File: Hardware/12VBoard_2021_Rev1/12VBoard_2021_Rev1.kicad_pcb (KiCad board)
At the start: 2 copper layers, 178 parts, among them Q1 2N7000, Q2 2N7000, Q3 NTR2101P, Q4 2N7000, Q5 2N7000, Q6 2N7000, Q7 2N7000, SW1 SW_SPDT, U1 LM2576SX-5.0/NOPB, U10 LM5116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

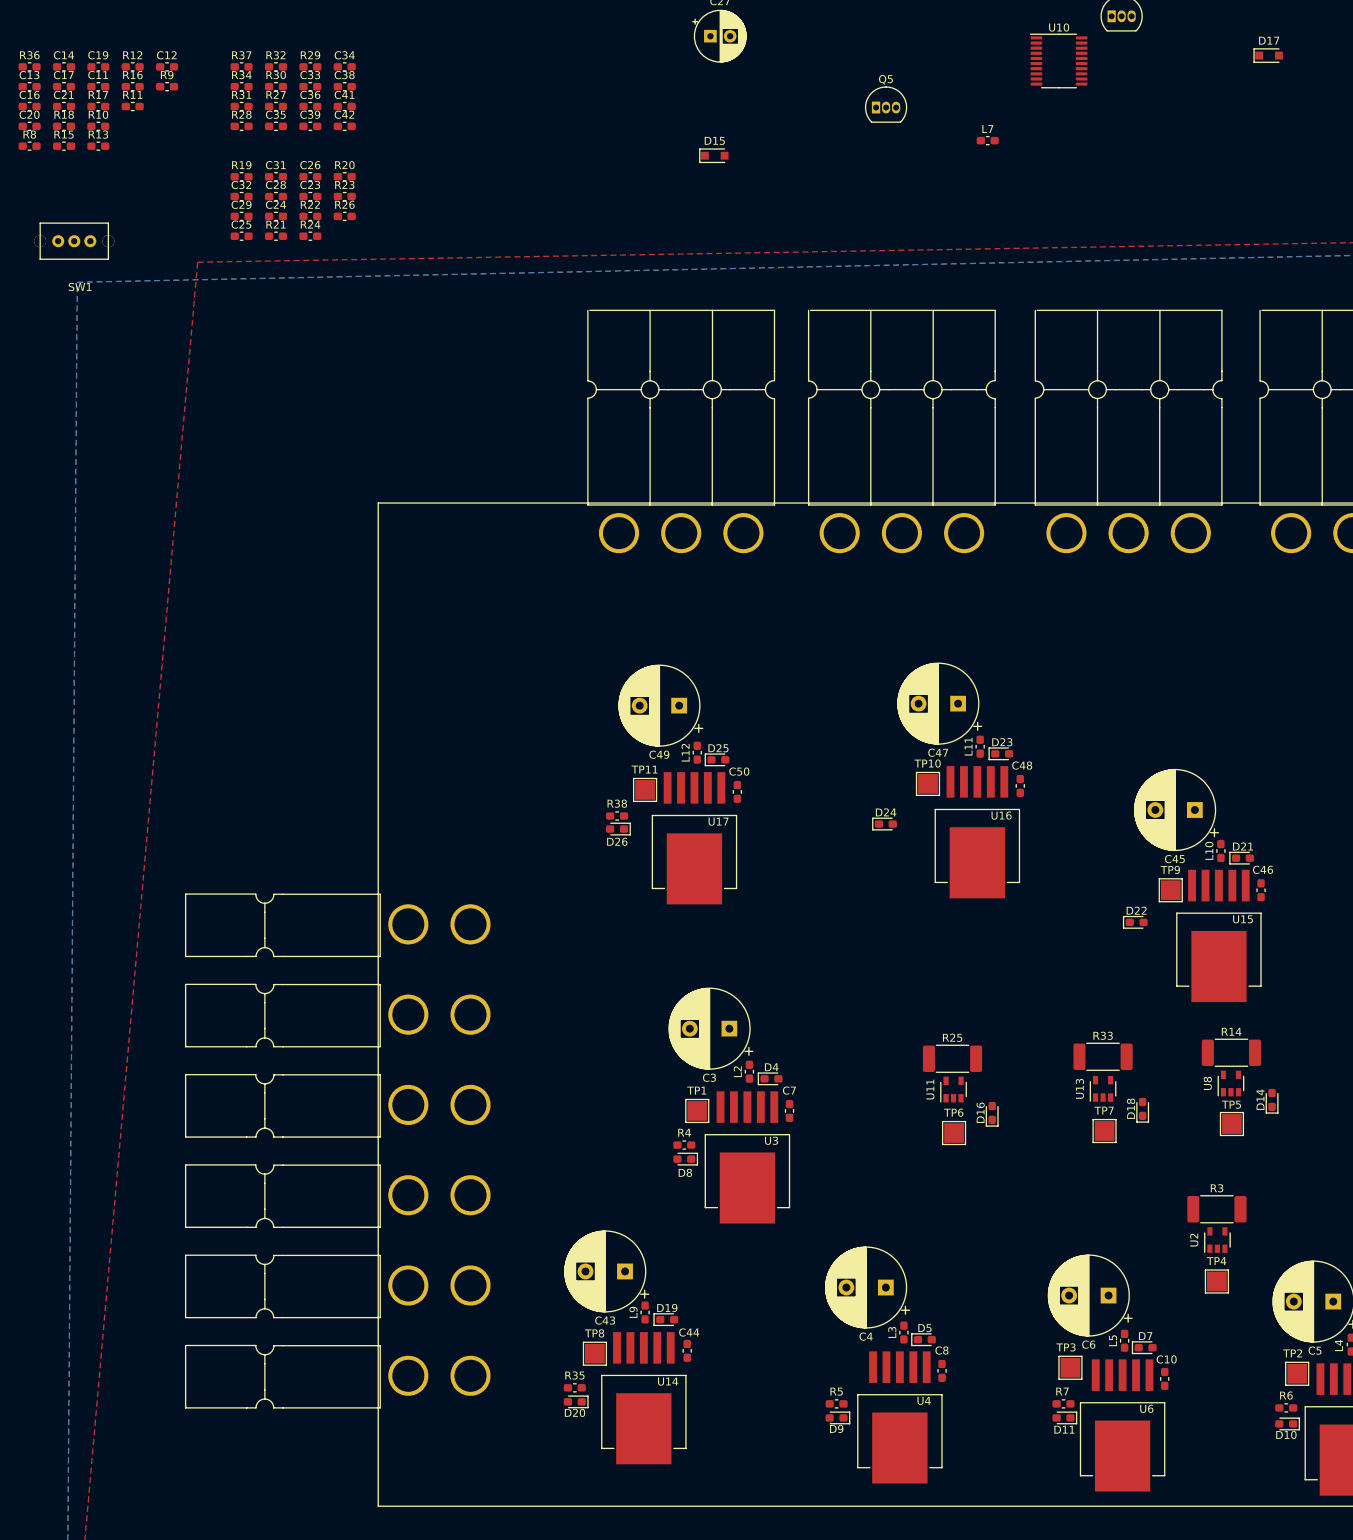
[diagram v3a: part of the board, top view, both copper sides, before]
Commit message: Fixed Nets for andersons
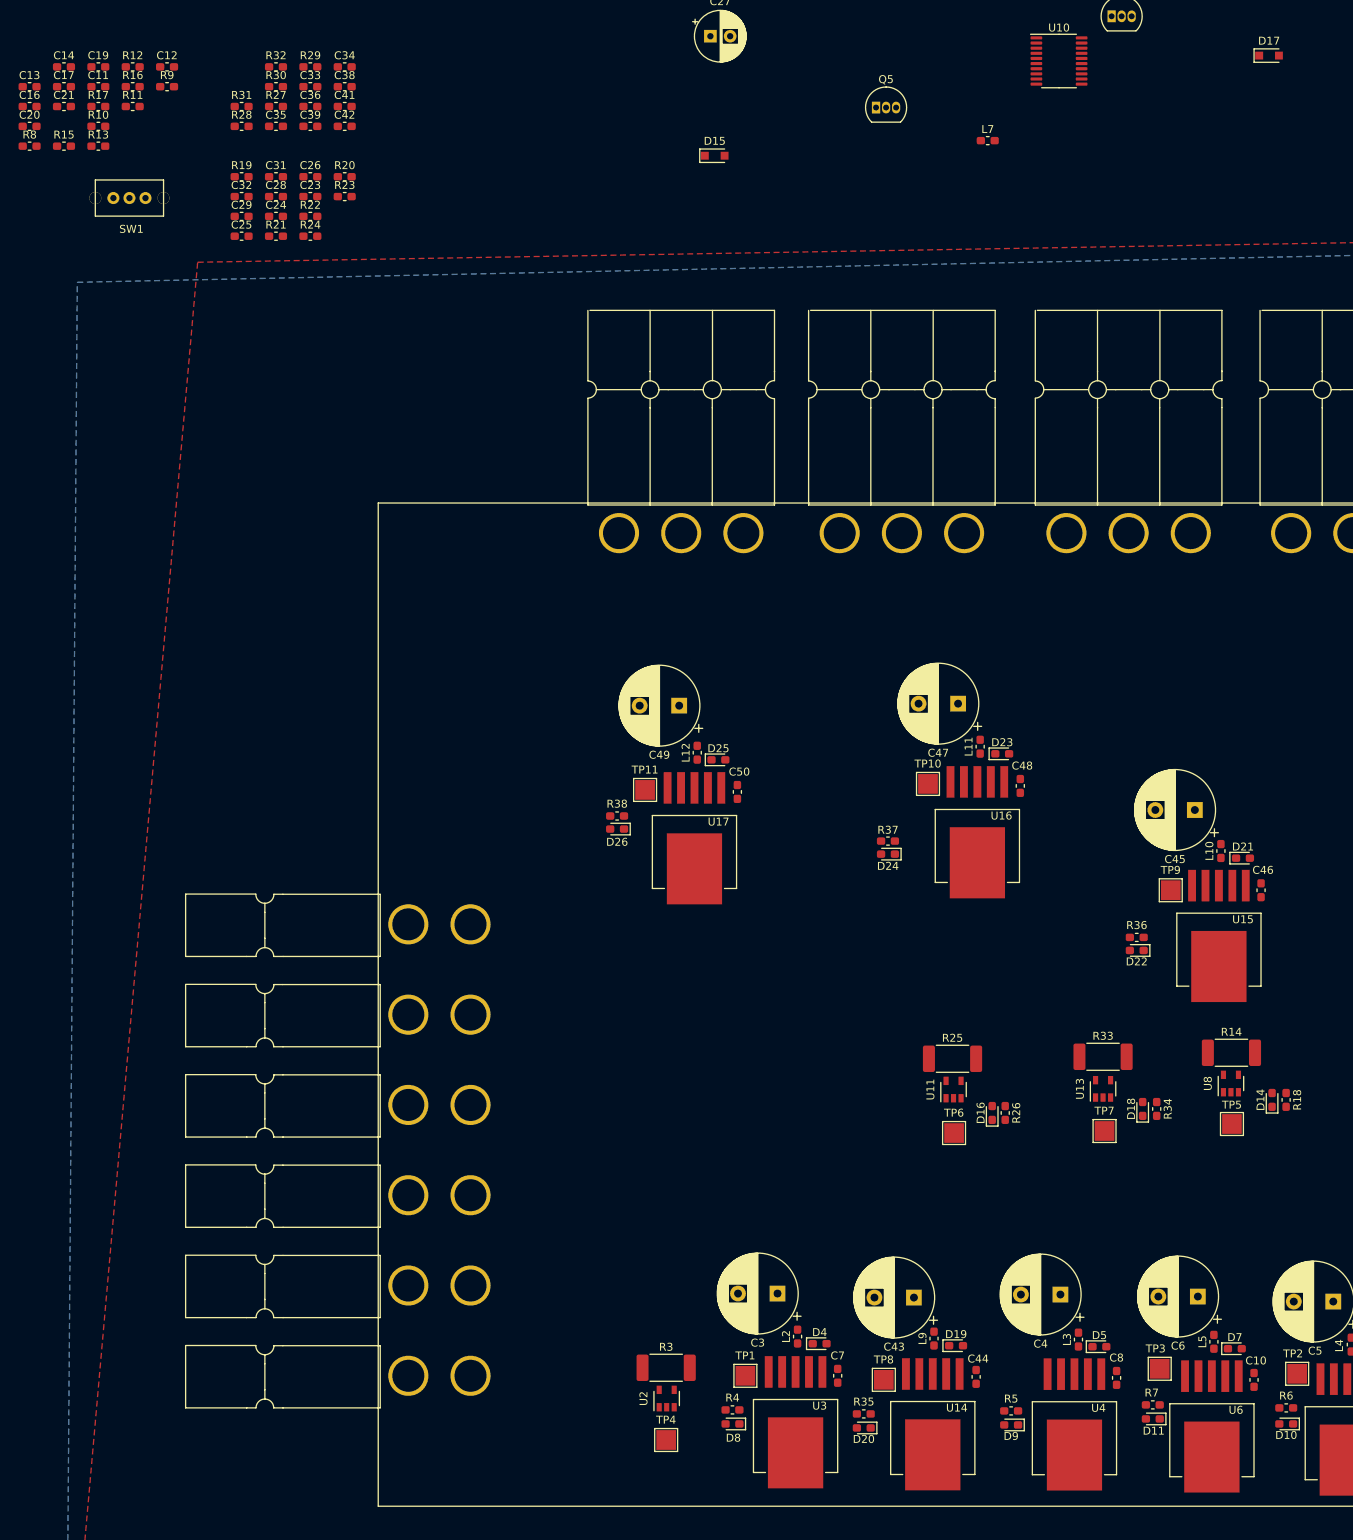
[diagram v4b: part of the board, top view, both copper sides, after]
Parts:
- moved R18 197.8 mm to (191.1, 98.4), turned to 270 degrees
- moved R36 178.3 mm to (172.2, 77.9), turned to 180 degrees
- moved R34 173.7 mm to (174.8, 99.6), turned to 270 degrees
- moved R26 141.0 mm to (155.6, 100.1), turned to 270 degrees
- moved R37 127.7 mm to (140.7, 65.7), turned to 180 degrees
- moved R3 72.6 mm to (112.6, 132.3)
- moved TP4 72.6 mm to (112.6, 141.5)
- moved U2 72.6 mm to (112.7, 136.2)
- moved C43 36.7 mm to (144.0, 123.4)
- moved D19 36.7 mm to (149.4, 129.5)
- moved D20 36.7 mm to (137.7, 140.0)
- moved R35 36.7 mm to (137.7, 138.2)
- moved C44 36.7 mm to (151.9, 133.5)
- moved L9 36.7 mm to (146.6, 128.6)
- moved TP8 36.7 mm to (140.2, 133.9)
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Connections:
- Conn15 pad 4: (no net) -> Net-(C43-Pad1)
- Conn4 pad 4: (no net) -> Net-(C4-Pad1)
- Conn5 pad 4: (no net) -> Net-(C3-Pad1)
- Conn6 pad 4: (no net) -> Net-(C5-Pad1)
- Conn7 pad 4: (no net) -> Net-(C6-Pad1)
- Conn8 pad 4: (no net) -> Net-(C6-Pad1)

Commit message: High side layout started with grouping components
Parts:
- moved U9 185.8 mm to (105.4, 39.9), turned to 90 degrees
- moved R25 175.3 mm to (316.8, 42.7)
- moved U11 175.3 mm to (316.9, 46.6)
- moved C18 173.7 mm to (138.2, 73.9)
- moved TP6 172.7 mm to (312.7, 47.2)
- moved D16 170.5 mm to (316.9, 49.8), turned to 180 degrees
- moved R33 169.8 mm to (330.0, 42.4)
- moved U13 169.8 mm to (330.0, 46.5)
- moved R26 168.4 mm to (316.9, 51.6), turned to 180 degrees
- moved TP7 167.1 mm to (325.9, 47.2)
- moved R14 165.3 mm to (341.7, 42.2)
- moved U8 165.3 mm to (341.6, 46.1)
- moved C15 165.3 mm to (128.3, 53.8)
- moved D18 164.8 mm to (329.9, 49.5), turned to 180 degrees
- moved TP5 162.8 mm to (337.8, 47.5)
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
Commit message: updated footprints
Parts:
- removed Q3: NTR2101P, Package_TO_SOT_SMD:SOT-23
- D1, D19, D21, D23, D25, D4, D5, D6, D7: footprint Diode_SMD:D_0603_1608Metric_Pad1.05x0.95mm_HandSolder -> Diode_THT:D_DO-201AD_P15.24mm_Horizontal
- Q1, Q4, Q6: value 2N7000 -> CSD18537NQ5A; footprint Package_TO_SOT_THT:TO-92_Inline -> Package_SON:VSONP-8-1EP_5x6_P1.27mm
- Q2, Q5, Q7: value 2N7000 -> CSD18531Q5A; footprint Package_TO_SOT_THT:TO-92_Inline -> Package_SON:VSONP-8-1EP_5x6_P1.27mm
- moved R18 262.8 mm to (79.1, 59.2)
- moved D14 262.7 mm to (79.1, 56.1)
- moved D18 251.1 mm to (78.9, 50.0)
- moved R34 250.8 mm to (79.1, 53.1)
- moved D16 237.9 mm to (79.2, 61.7)
- moved R26 237.9 mm to (79.4, 65.3)
- moved R23 161.8 mm to (206.1, 74.4)
- moved C25 161.5 mm to (193.0, 79.0)
- moved C29 161.5 mm to (193.0, 76.5)
- moved C32 161.5 mm to (193.0, 74.0)
- moved R19 161.5 mm to (193.0, 71.5)
- moved C23 161.5 mm to (201.7, 74.0)
- moved C24 161.5 mm to (197.4, 76.5)
- moved C26 161.5 mm to (201.7, 71.5)
- moved C28 161.5 mm to (197.4, 74.0)
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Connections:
- Q1 pad 2: HO -> SW
- Q1 pad 3: /High Current Outputs/Multimedia/Extra/PackVoltage -> SW
- Q2 pad 2: LO -> (no net)
- Q2 pad 3: SW -> CS
- Q4 pad 2: HO -> SW
- Q4 pad 3: /High Current Outputs/AuxMount/PackVoltage -> SW
- Q5 pad 2: LO -> (no net)
- Q5 pad 3: SW -> CS
- Q6 pad 2: HO -> SW
- Q6 pad 3: /High Current Outputs/PackVoltage -> SW
- Q7 pad 2: LO -> (no net)
- Q7 pad 3: SW -> CS

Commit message: Layout kinda finished
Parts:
- added Q3: IRFZ34, Package_TO_SOT_THT:TO-220-3_Vertical, F.Cu at (111.9, 55.8)
- moved TP5 203.0 mm to (135.0, 55.9)
- moved R14 199.6 mm to (142.6, 55.8)
- moved U8 199.6 mm to (142.5, 59.6)
- moved C45 176.0 mm to (142.1, 94.4), turned to 0 degrees
- moved TP9 173.3 mm to (136.4, 101.5)
- moved L10 172.6 mm to (136.3, 113.9)
- moved C46 172.4 mm to (136.3, 110.9)
- moved D22 172.1 mm to (136.3, 107.8), turned to 0 degrees
- moved R36 171.9 mm to (136.3, 104.8)
- moved U15 171.7 mm to (144.8, 109.3)
- moved TP7 163.4 mm to (162.7, 56.0)
- moved R33 161.2 mm to (169.4, 56.0)
- moved U13 161.2 mm to (169.4, 60.1)
- moved D21 153.2 mm to (154.4, 113.9), turned to 90 degrees
- moved C47 139.5 mm to (165.5, 95.8), turned to 0 degrees
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
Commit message: Started Laying out bucks
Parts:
- moved C12 571.2 mm to (718.1, 73.9)
- moved C14 571.2 mm to (709.2, 60.5)
- moved C18 571.2 mm to (701.8, 72.4)
- moved C23 571.2 mm to (772.7, 74.3)
- moved C24 571.2 mm to (763.8, 60.8)
- moved C25 571.2 mm to (764.0, 77.5)
- moved C26 571.2 mm to (768.4, 60.8)
- moved C27 571.2 mm to (757.1, 64.4)
- moved C29 571.2 mm to (768.6, 71.0)
- moved C30 571.2 mm to (757.0, 73.0)
- moved C32 571.2 mm to (763.8, 64.1)
- moved C34 571.2 mm to (736.6, 60.7)
- moved C36 571.2 mm to (740.9, 60.7)
- moved C37 571.2 mm to (729.4, 73.2)
- moved C38 571.2 mm to (736.6, 67.3)
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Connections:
- C44 pad 1: Net-(C44-Pad1) -> Net-(C10-Pad1)
- U14 pad 1: Net-(C44-Pad1) -> Net-(C10-Pad1)
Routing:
- net Net-(C3-Pad1): track 0.00 -> 134.0 mm, vias 0 -> 1
- net Net-(C10-Pad1): track 0.00 -> 84.6 mm, vias 0 -> 2
- net /High Current Outputs/PackVoltage: track 6.46 -> 53.3 mm
- net Net-(C43-Pad1): track 0.00 -> 42.4 mm
- net /High Current Outputs/5V: track 0.00 -> 40.9 mm
- net Net-(C6-Pad1): track 0.00 -> 34.5 mm
- net Net-(D7-Pad1): track 0.00 -> 30.3 mm, vias 0 -> 2
- net Net-(D19-Pad1): track 0.00 -> 28.6 mm
- net Net-(D4-Pad1): track 0.00 -> 23.0 mm
- net Net-(D1-Pad1): track 0.00 -> 21.2 mm
- net /Tiva In/Outputs/CameraCTL: track 0.00 -> 13.9 mm, vias 0 -> 2
- net /Low Current Outputs/DriveCTL: track 0.00 -> 12.6 mm, vias 0 -> 2
- net /Tiva In/Outputs/ExtraCTL: track 0.00 -> 4.47 mm
- net /Low Current Outputs/CurrentSense: track 0.00 -> 3.13 mm
- net Net-(D2-Pad2): track 4.32 -> 1.79 mm
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- added copper zone on B.Cu, net /High Current Outputs/PackVoltage
- added copper zone on F.Cu, net /High Current Outputs/PackVoltage
- added copper zone on F.Cu, net Net-(C10-Pad1)
- added copper zone on B.Cu, net Net-(C6-Pad1)
- added copper zone on F.Cu, net Net-(C6-Pad1)
